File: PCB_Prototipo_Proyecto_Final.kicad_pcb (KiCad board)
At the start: 2 copper layers, 165.1 x 154.9 mm, 152 parts, among them IC1 UA741CP, J1 VIN, J10 Terminal_Sensores_Nivel, J11 Terminal_Sensor_Flujo, J12 Rele_4, J13 Rele_7, J14 Rele_1, J15 Rele_5, J16 Rele_2, J17 Rele_3, J18 Rele_6, J19 Pin GND, J2 Conn_01x15, J20 Conector 3V3, J21 Conector GND, J22 Pin_3V3, J23 Pin_3V3, J24 Pin GND, J25 Pin_3V3, J26 Pin GND, J27 Pin_3V3, J28 Pin_3V3, J29 Pin_3V3, J3 Conn_01x15, J30 Pin GND, J31 Pin GND, J32 Pin GND, J33 Pin GND, J34 Pin GND, J35 Pin GND, J36 Pin GND, J37 Pin GND, J38 Pin GND, J39 Pin GND, J4 Terminal_Sensor_pH, J40 Pin GND, J41 Pin GND, J42 Pin GND, J43 Conector GND, J5 Terminal_Sensor_CO2, J6 Terminal_Sensor_TDS, J7 Terminal_Sensor_Temp_Sumerg, J8 Terminal_Sensor_Iluminacion, J9 Terminal_Sensor_Temp_y_Hum, K1 SRD-05VDC-SL-C, K2 SRD-05VDC-SL-C, K3 SRD-05VDC-SL-C, K4 SRD-05VDC-SL-C, K5 SRD-05VDC-SL-C, K6 SRD-05VDC-SL-C, K7 SRD-05VDC-SL-C, Q1 2N7002, Q10 2N7002, Q11 2N7002, Q12 2N7002, Q13 2N7002, Q14 2N7002, Q15 2N7002, Q2 2N7002, Q3 2N7002, Q4 2N7002, Q5 2N7002, Q6 2N7002, Q7 2N7002, Q8 2N7002, Q9 2N7002, U1 LM2596S-5, U2 LM1117-3.3, U3 MCP23008-xP

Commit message: Continuación de rerouteo.
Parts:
- J30, J31, J32, J33, J35, J36: moved to F.Cu
- moved Q10 10.7 mm to (159.6, 94.2)
- moved R44 10.7 mm to (272.5, 94.0)
- moved R49 9.90 mm to (232.7, 94.0)
- moved R48 9.82 mm to (252.7, 94.0)
- moved R42 9.26 mm to (212.1, 94.0)
- moved R50 8.91 mm to (171.6, 94.2)
- moved R45 8.47 mm to (192.6, 94.2)
- moved J31 8.13 mm to (272.5, 88.6), turned to 0 degrees
- moved D7 8.11 mm to (240.5, 88.6), turned to 0 degrees
- moved D5 7.98 mm to (200.2, 88.8), turned to 0 degrees
- moved D8 7.85 mm to (180.0, 88.7), turned to 0 degrees
- moved J36 7.79 mm to (171.7, 88.8), turned to 0 degrees
- moved D6 7.77 mm to (260.4, 88.6), turned to 0 degrees
- moved D4 7.68 mm to (280.2, 88.6), turned to 0 degrees
- moved J32 7.24 mm to (192.5, 88.8), turned to 0 degrees
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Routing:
- net /Microcontrolador/Rele_1: track 31.5 -> 0.00 mm
- net /Microcontrolador/Rele_2: track 27.9 -> 0.00 mm
- net /Microcontrolador/Rele_6: track 26.9 -> 0.00 mm
- net /Microcontrolador/Rele_3: track 25.9 -> 0.00 mm
- net /Microcontrolador/Rele_5: track 25.1 -> 0.00 mm
- net +5V: track 147.8 -> 123.0 mm
- net /Microcontrolador/Rele_4: track 23.8 -> 0.00 mm
- net Net-(D4-Pad2): track 23.3 -> 0.00 mm
- net Net-(D5-Pad2): track 22.2 -> 0.31 mm
- net Net-(D7-Pad2): track 21.8 -> 0.00 mm
- net Net-(D6-Pad2): track 21.4 -> 0.00 mm
- net Net-(D2-Pad2): track 20.6 -> 0.31 mm
- net Net-(D8-Pad2): track 11.3 -> 0.80 mm

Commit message: Finalización de rerouteo de PCB.
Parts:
- removed REF**: MountingHole_3.5mm_Pad, MountingHole:MountingHole_3.5mm_Pad
- added ?: , , F.Cu at (292.4, 58.2)
- added J44: Pin GND, Connector_PinHeader_2.54mm:PinHeader_1x01_P2.54mm_Vertical, F.Cu at (151.9, 88.9)
- added J45: Pin_3V3, Connector_PinHeader_2.54mm:PinHeader_1x01_P2.54mm_Vertical, F.Cu at (156.0, 178.1)
- ? (x2): moved to F.Cu
- J19: value Pin GND -> Pin_3V3
- moved J19 46.4 mm to (151.4, 115.1)
- moved J20 39.6 mm to (250.7, 166.9)
- moved R47 16.0 mm to (223.5, 137.6)
- moved J21 6.34 mm to (250.2, 108.2)
- moved C20 3.13 mm to (199.4, 106.4), turned to 180 degrees
- moved J34 2.98 mm to (232.2, 113.3)
- moved C19 2.31 mm to (199.3, 104.1), turned to 180 degrees
- moved R46 1.94 mm to (234.5, 130.0), turned to 90 degrees
- turned ? to 0 degrees (x2)
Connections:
- J19 pad 1: GND -> +3.3V
- J2 pad 11: /Microcontrolador/SensorNivel_4 -> /Microcontrolador/SensorNivel_2
- J2 pad 12: /Microcontrolador/SensorNivel_5 -> /Microcontrolador/SensorNivel_1
- J2 pad 8: /Microcontrolador/SensorNivel_1 -> /Microcontrolador/SensorNivel_5
- J2 pad 9: /Microcontrolador/SensorNivel_2 -> /Microcontrolador/SensorNivel_4
- U3 pad 10: /Microcontrolador/Rele_7 -> /Microcontrolador/Rele_1
- U3 pad 11: /Microcontrolador/Rele_6 -> /Microcontrolador/Rele_2
- U3 pad 12: /Microcontrolador/Rele_5 -> /Microcontrolador/Rele_3
- U3 pad 14: /Microcontrolador/Rele_3 -> /Microcontrolador/Rele_5
- U3 pad 15: /Microcontrolador/Rele_2 -> /Microcontrolador/Rele_6
- U3 pad 16: /Microcontrolador/Rele_1 -> /Microcontrolador/Rele_7
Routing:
- net +5V: track 123.0 -> 618.1 mm
- net +3.3V: track 67.4 -> 413.2 mm
- net /Microcontrolador/Rele_7: track 0.00 -> 70.1 mm
- net /Microcontrolador/Rele_1: track 0.00 -> 63.6 mm
- net /Microcontrolador/Trigger__pH: track 0.00 -> 62.6 mm
- net /Microcontrolador/MCP23008_SCL: track 0.00 -> 62.3 mm
- net /Entradas/Data_SensorTempSumerg: track 0.00 -> 60.0 mm
- net /Entradas/Ilum_Analog: track 0.00 -> 54.2 mm
- net /Entradas/TDS_Analog: track 0.00 -> 54.0 mm
- net /Entradas/Data_SensorTempHum: track 0.00 -> 53.0 mm
- net /Microcontrolador/Rele_6: track 0.00 -> 52.0 mm
- net /Microcontrolador/SensorNivel_5: track 15.6 -> 67.0 mm
- net /Microcontrolador/SensorFlujo: track 0.00 -> 49.1 mm
- net /Microcontrolador/Rele_2: track 0.00 -> 47.7 mm
- net /Microcontrolador/SensorCO2: track 9.03 -> 55.5 mm
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
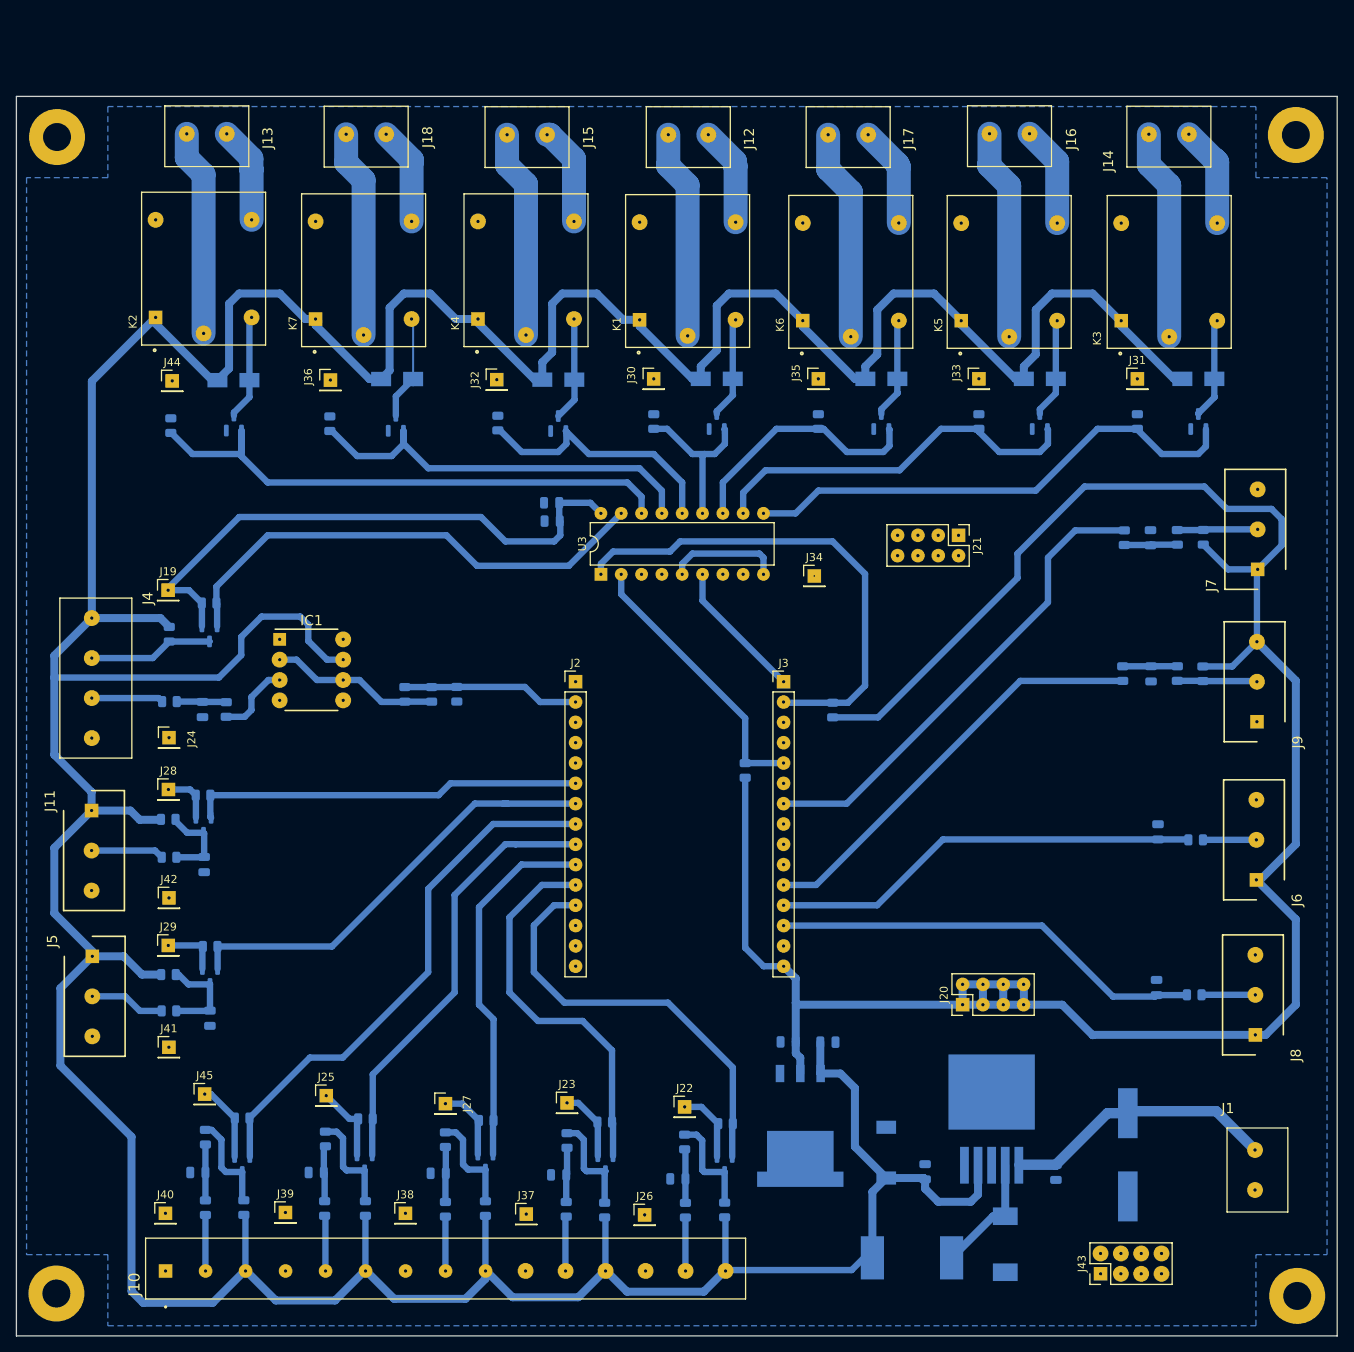
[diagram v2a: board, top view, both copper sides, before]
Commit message: Correccion footprints
Se realizo el cambio de algunas footprints segun los componentes disponibles, como los capacitores de 470 uF o la inductancia de la fte switching, y tambien se cambio el LM2596 por el modelo ADJ, con el agregado de un divisor resistivo.
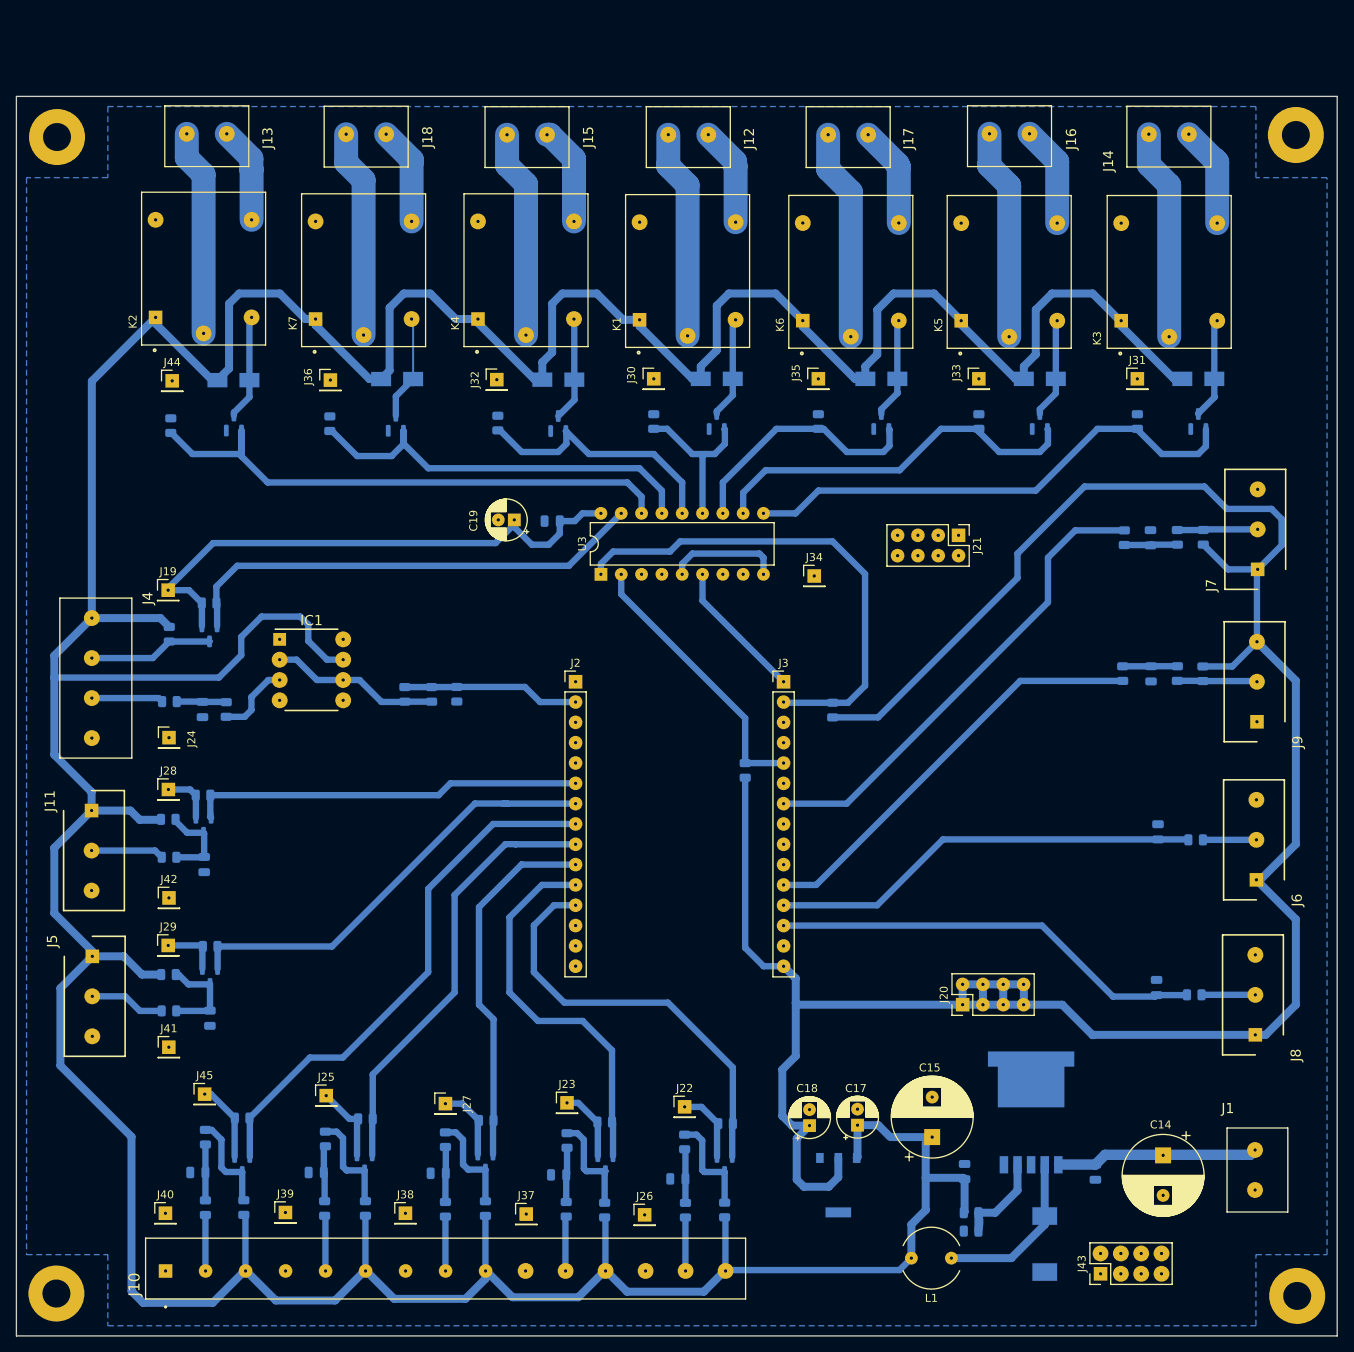
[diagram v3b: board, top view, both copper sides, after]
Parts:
- added R51: 3,3K, 1/8W, Resistor_SMD:R_0805_2012Metric, B.Cu at (251.8, 195.2)
- added R52: 10K, 1/8W, Resistor_SMD:R_0805_2012Metric, B.Cu at (251.8, 192.9)
- C14: footprint VE-471M1HTR-1316:CAPAE1300X1650N -> Capacitor_THT:CP_Radial_D10.0mm_P5.00mm; moved to F.Cu
- C15: footprint TPSE227K010R0100:TPSE227K016R0100V -> Capacitor_THT:CP_Radial_D10.0mm_P5.00mm; moved to F.Cu
- C17, C18, C19: footprint Capacitor_SMD:C_0805_2012Metric -> Capacitor_THT:CP_Radial_D5.0mm_P2.00mm; moved to F.Cu
- L1: footprint 7447709470:WE-PD_1260_1245_1280_121054 -> Inductor_THT:L_Radial_D7.5mm_P5.00mm_Fastron_07P; moved to F.Cu
- U1: value LM2596S-5 -> LM2596S-ADJ; footprint Package_TO_SOT_SMD:TO-263-5_TabPin3 -> LM2596SX-ADJ_NOPB:LM2596SXADJNOPB
- U2: footprint LM1117SX-3V3-NOPB:KTT0003B -> LM1117MPX-33NOPB:SOT230P700X180-4N
- moved C17 11.0 mm to (237.6, 181.9), turned to 90 degrees
- moved C18 10.8 mm to (231.6, 182.0), turned to 90 degrees
- moved C15 6.07 mm to (246.9, 183.4)
- moved C19 5.13 mm to (194.7, 106.3)
- moved U1 4.94 mm to (259.3, 181.4), turned to -90 degrees
- moved C13 4.94 mm to (267.3, 187.8)
- moved C16 4.94 mm to (250.9, 187.7)
- moved D1 4.94 mm to (261.0, 196.8)
- moved L1 4.93 mm to (249.3, 198.6)
- moved U2 4.92 mm to (235.2, 189.4), turned to -90 degrees
- moved C14 4.41 mm to (275.8, 185.7)
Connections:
- U1 pad 4: +5V -> Net-(U1-Pad4)
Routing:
- net +3.3V: track 413.2 -> 436.9 mm
- net Net-(U1-Pad4): track 0.00 -> 13.9 mm
- net /Fuentes/VIN_24V: track 34.1 -> 25.3 mm
- net +5V: track 618.1 -> 612.2 mm
- net Net-(D1-Pad1): track 15.2 -> 20.9 mm
- net /Microcontrolador/Trigger__pH: track 62.6 -> 59.4 mm

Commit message: Corrección de PCB.
Se agregaron algunos pin headers para conectar a GND algunos puntos. Se generaron los Gerber finales.
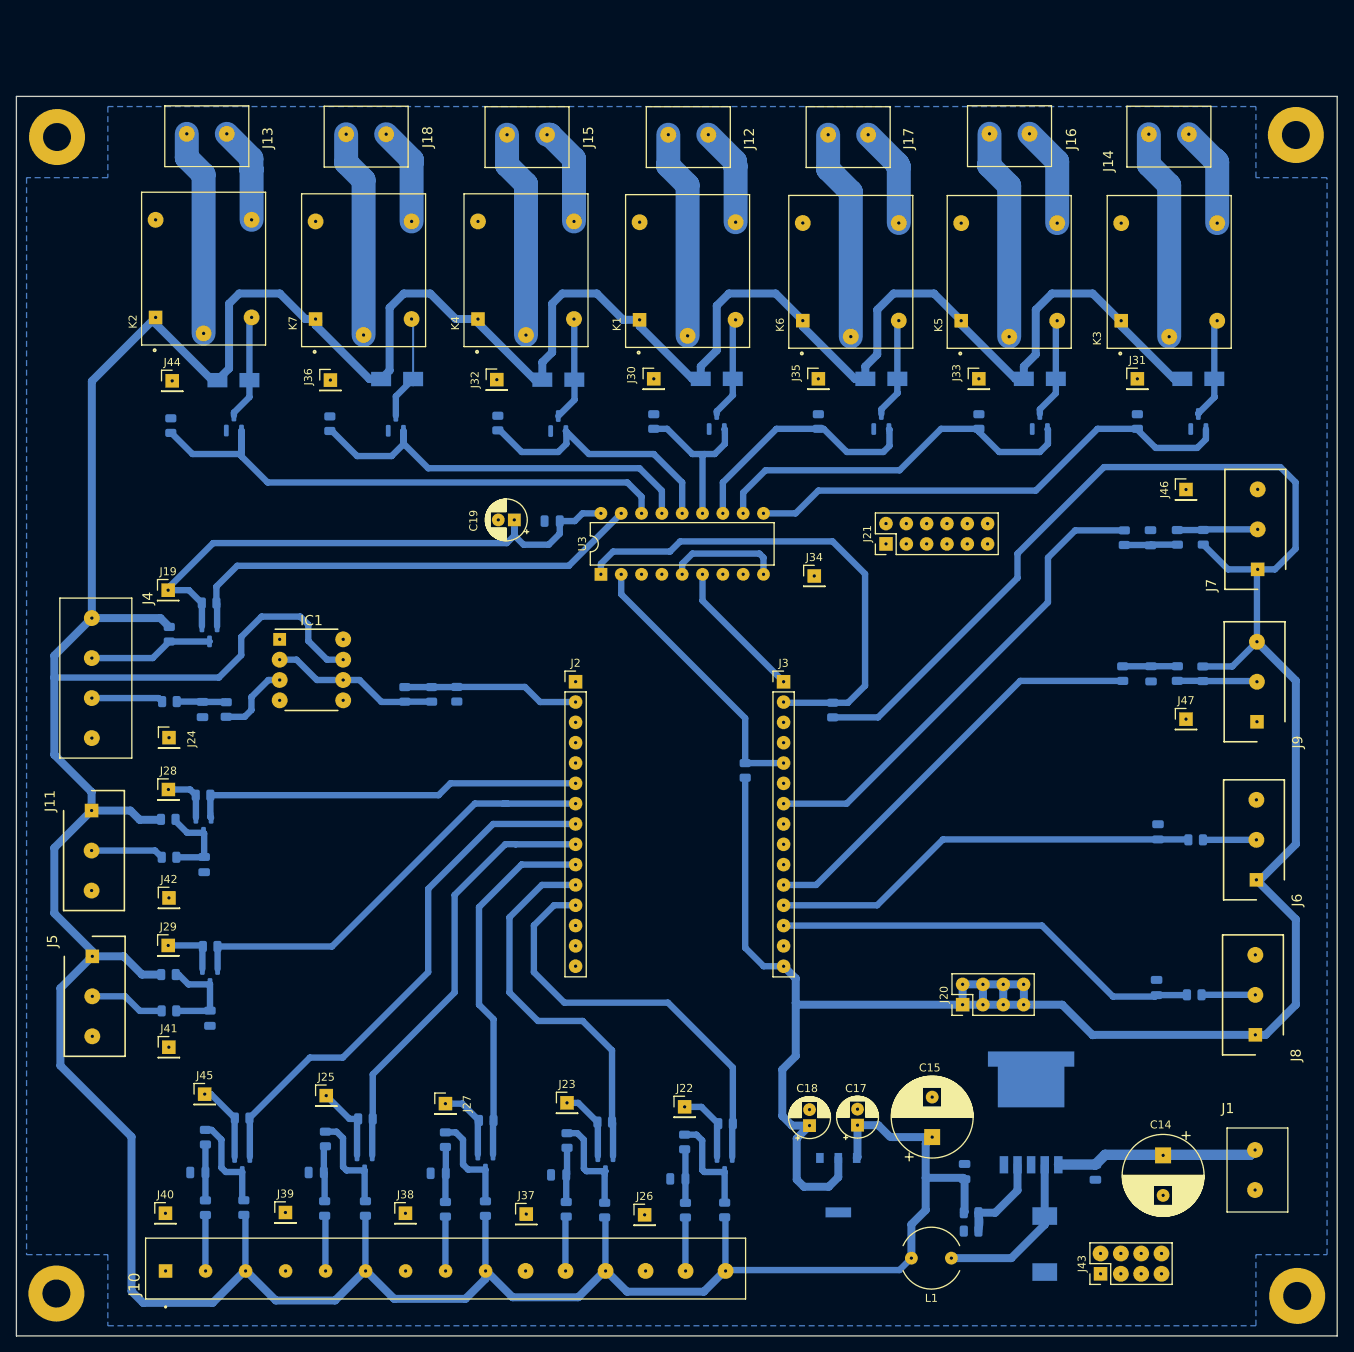
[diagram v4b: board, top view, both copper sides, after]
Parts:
- added J46: Pin GND, Connector_PinHeader_2.54mm:PinHeader_1x01_P2.54mm_Vertical, F.Cu at (278.6, 102.5)
- added J47: Pin GND, Connector_PinHeader_2.54mm:PinHeader_1x01_P2.54mm_Vertical, F.Cu at (278.6, 131.2)
- J21: footprint Connector_PinHeader_2.54mm:PinHeader_2x04_P2.54mm_Vertical -> Connector_PinHeader_2.54mm:PinHeader_2x06_P2.54mm_Vertical
- moved J21 9.13 mm to (241.1, 109.3), turned to 90 degrees
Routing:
- net +3.3V: track 436.9 -> 446.8 mm
- net /Microcontrolador/Rele_1: track 63.6 -> 62.5 mm
